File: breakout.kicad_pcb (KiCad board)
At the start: 2 copper layers, 25.9 x 20.8 mm, 12 parts, among them P1 CONN_01X08, P2 CONN_01X08, U1 ESP-12E, U2 APE8865Y5-33-HF-3

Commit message: Make vias a bit prettier.
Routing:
- net GND: track 29.0 -> 25.1 mm
- net /3V3: track 39.7 -> 43.2 mm
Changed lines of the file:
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@@
-(kicad_pcb (version 4) (host pcbnew 0.201512291232+6408~40~ubuntu15.04.1-stable)
+(kicad_pcb (version 4) (host pcbnew 4.0.1-3.201512221402+6198~38~ubuntu15.04.1-stable)
   (general
     (links 33)
     (no_connects 0)
-    (area 121.891667 43.899799 154.968334 74.325)
+    (area 125.400999 51.486999 151.459001 72.465001)
     (thickness 1.6)
     (drawings 31)
-    (tracks 144)
+    (tracks 148)
     (zones 0)
     (modules 12)
@@
     (fp_line (start -1.55 0) (end -1.55 1.55) (layer B.SilkS) (width 0.15))
     (fp_line (start -1.55 1.55) (end 1.55 1.55) (layer B.SilkS) (width 0.15))
-    (pad 1 thru_hole rect (at 0 0 180) (size 2.032 1.7272) (drill 1.016) (layers *.Cu *.Mask B.SilkS)
+    (pad 1 thru_hole oval (at 0 0 180) (size 2.032 1.7272) (drill 1.016) (layers *.Cu *.Mask B.SilkS)
       (net 1 "Net-(P1-Pad1)"))
     (pad 2 thru_hole oval (at 0 -2.54 180) (size 2.032 1.7272) (drill 1.016) (layers *.Cu *.Mask B.SilkS)
@@
   (segment (start 127.13 71.25) (end 127 71.12) (width 0.5) (layer F.Cu) (net 15) (status 30))
   (segment (start 137.01 71.12) (end 137.33 70.8) (width 0.5) (layer B.Cu) (net 15) (status 30))
-  (segment (start 146.456 66.576) (end 141.576 66.576) (width 0.5) (layer F.Cu) (net 16))
-  (segment (start 141.576 66.576) (end 141.25 66.25) (width 0.5) (layer F.Cu) (net 16))
-  (via (at 141.25 66.25) (size 1.2) (drill 0.75) (layers F.Cu B.Cu) (net 16))
-  (segment (start 146.12 71.12) (end 141.25 66.25) (width 0.5) (layer B.Cu) (net 16))
-  (segment (start 141.25 66.25) (end 140.9 65.9) (width 0.5) (layer B.Cu) (net 16))
+  (segment (start 144.741474 68.44) (end 145.590002 68.44) (width 0.5) (layer B.Cu) (net 16))
+  (segment (start 144.69 68.44) (end 144.741474 68.44) (width 0.5) (layer B.Cu) (net 16))
+  (segment (start 146.456 66.576) (end 146.456 67.626) (width 0.5) (layer F.Cu) (net 16))
+  (segment (start 148.270002 71.12) (end 146.190001 69.039999) (width 0.5) (layer B.Cu) (net 16))
+  (segment (start 141 64.75) (end 144.69 68.44) (width 0.5) (layer B.Cu) (net 16))
+  (segment (start 145.642 68.44) (end 145.590002 68.44) (width 0.5) (layer F.Cu) (net 16))
+  (segment (start 149.86 71.12) (end 148.270002 71.12) (width 0.5) (layer B.Cu) (net 16))
+  (segment (start 146.456 67.626) (end 145.642 68.44) (width 0.5) (layer F.Cu) (net 16))
+  (segment (start 140.9 64.75) (end 141 64.75) (width 0.5) (layer B.Cu) (net 16))
+  (segment (start 146.190001 69.039999) (end 145.590002 68.44) (width 0.5) (layer B.Cu) (net 16))
+  (via (at 145.590002 68.44) (size 1.2) (drill 0.75) (layers F.Cu B.Cu) (net 16))
   (segment (start 137.33 69.85) (end 136.614998 69.85) (width 0.5) (layer B.Cu) (net 16))
   (segment (start 136.614998 69.85) (end 135.87 69.105002) (width 0.5) (layer B.Cu) (net 16))
   (segment (start 135.87 69.105002) (end 135.87 65.895) (width 0.5) (layer B.Cu) (net 16))
   (segment (start 135.87 65.895) (end 135.87 64.77) (width 0.5) (layer B.Cu) (net 16))
-  (segment (start 149.86 71.12) (end 146.12 71.12) (width 0.5) (layer B.Cu) (net 16))
-  (segment (start 140.9 65.9) (end 140.9 64.75) (width 0.5) (layer B.Cu) (net 16))
   (segment (start 140.9 64.75) (end 135.89 64.75) (width 0.5) (layer B.Cu) (net 16) (status 30))
   (segment (start 135.89 64.75) (end 135.87 64.77) (width 0.5) (layer B.Cu) (net 16) (status 30))
-  (segment (start 149.86 71.12) (end 149.7076 71.12) (width 0.5) (layer B.Cu) (net 16) (status 30))
   (segment (start 140.97 64.77) (end 140.87 64.77) (width 0.5) (layer B.Cu) (net 16) (status 30))
-  (segment (start 132.5 66.5) (end 132.5 65.64) (width 0.5) (layer B.Cu) (net 17))
-  (segment (start 132.5 65.64) (end 133.37 64.77) (width 0.5) (layer B.Cu) (net 17))
-  (segment (start 130.456 66.576) (end 132.424 66.576) (width 0.5) (layer F.Cu) (net 17))
-  (segment (start 132.424 66.576) (end 132.5 66.5) (width 0.5) (layer F.Cu) (net 17))
-  (via (at 132.5 66.5) (size 1.2) (drill 0.75) (layers F.Cu B.Cu) (net 17))
+  (segment (start 131.67 67.93) (end 131.67 66.47) (width 0.5) (layer B.Cu) (net 17))
+  (segment (start 131.67 66.47) (end 133.37 64.77) (width 0.5) (layer B.Cu) (net 17))
+  (segment (start 131.69 70.29) (end 131.69 67.95) (width 0.5) (layer F.Cu) (net 17))
+  (segment (start 131.69 67.95) (end 131.67 67.93) (width 0.5) (layer F.Cu) (net 17))
+  (via (at 131.67 67.93) (size 1.2) (drill 0.75) (layers F.Cu B.Cu) (net 17))
+  (segment (start 132.65 71.25) (end 131.69 70.29) (width 0.5) (layer F.Cu) (net 17))
   (segment (start 133.2405 64.8995) (end 133.37 64.77) (width 0.5) (layer B.Cu) (net 17))
   (via (at 134.75 71.25) (size 1.2) (drill 0.75) (layers F.Cu B.Cu) (net 17))

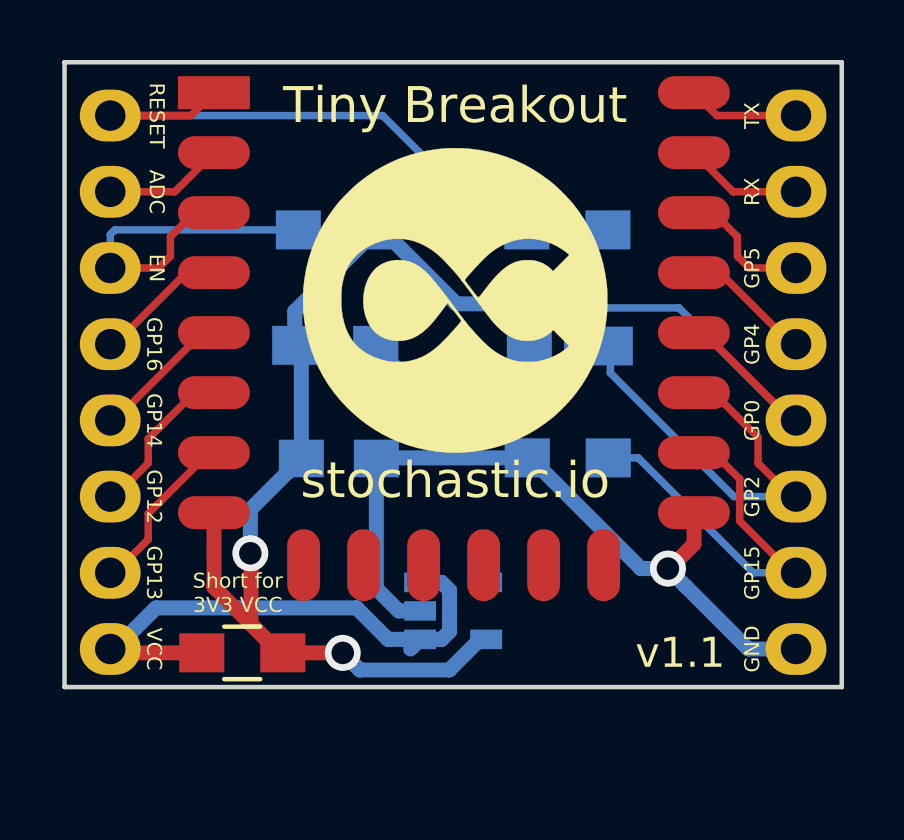
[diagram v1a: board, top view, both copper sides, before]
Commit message: Delete rogue tracks.
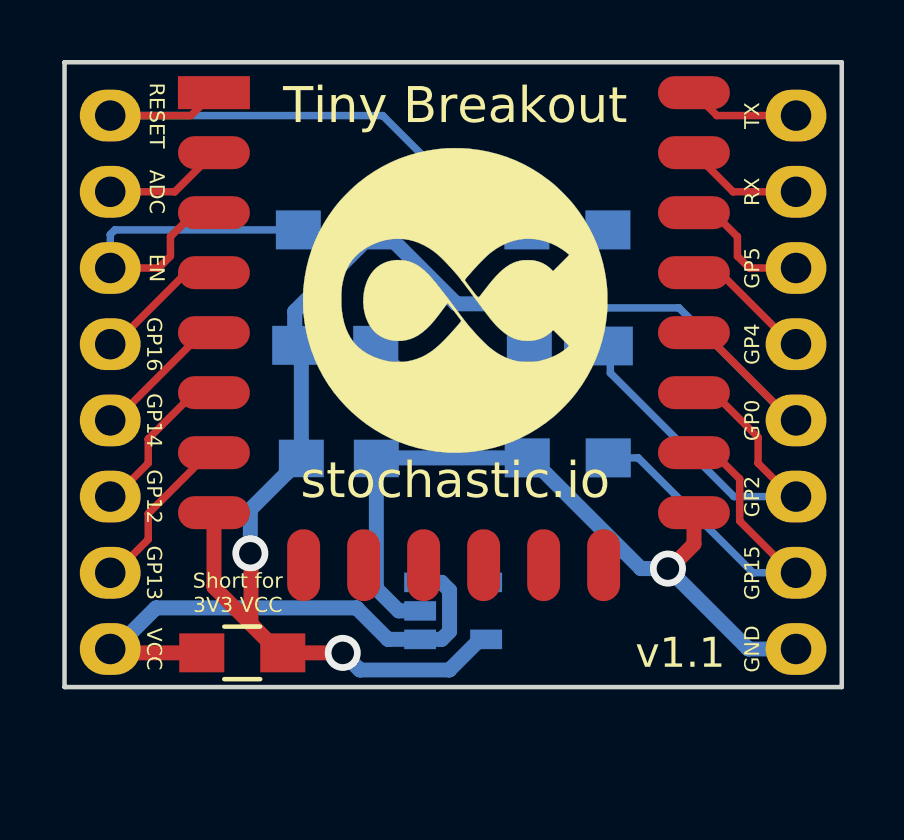
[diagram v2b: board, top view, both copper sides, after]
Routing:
- net Net-(P2-Pad5): track 24.9 -> 24.2 mm
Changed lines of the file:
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@@
     (links 33)
     (no_connects 0)
-    (area 125.400999 51.486999 151.459001 72.465001)
+    (area 121.891667 43.899799 154.968334 74.325)
     (thickness 1.6)
     (drawings 31)
-    (tracks 148)
+    (tracks 143)
     (zones 0)
     (modules 12)
@@
     (visible_elements FFFFFF7F)
     (pcbplotparams
-      (layerselection 0x010f0_ffffffff)
+      (layerselection 0x010f0_80000001)
       (usegerberextensions true)
       (excludeedgelayer true)
@@
       (drillshape 0)
       (scaleselection 1)
-      (outputdirectory ../../gerbs/))
+      (outputdirectory /home/stavros/Desktop/gerbs/))
   )
   (net 0 "")
@@
   (segment (start 147.3236 58.576) (end 146.456 58.576) (width 0.25) (layer F.Cu) (net 11) (status 30))
   (segment (start 142.954998 59.75) (end 145.9576 59.75) (width 0.25) (layer B.Cu) (net 12))
-  (segment (start 145.9576 59.75) (end 149.7076 63.5) (width 0.25) (layer B.Cu) (net 12))
-  (segment (start 149.7076 63.5) (end 149.86 63.5) (width 0.25) (layer B.Cu) (net 12))
+  (segment (start 145.9576 59.75) (end 149.7076 63.5) (width 0.25) (layer B.Cu) (net 12) (status 20))
+  (segment (start 149.7076 63.5) (end 149.86 63.5) (width 0.25) (layer B.Cu) (net 12) (status 30))
   (segment (start 142.25 62.275) (end 142.25 60.454998) (width 0.25) (layer B.Cu) (net 12))
   (segment (start 142.25 60.454998) (end 142.954998 59.75) (width 0.25) (layer B.Cu) (net 12))
-  (segment (start 135.85 61) (end 135.95 61) (width 0.25) (layer B.Cu) (net 12))
-  (segment (start 135.95 61) (end 137.95 63) (width 0.25) (layer B.Cu) (net 12))
+  (segment (start 135.85 61) (end 135.95 61) (width 0.25) (layer B.Cu) (net 12) (status 30))
+  (segment (start 135.95 61) (end 137.95 63) (width 0.25) (layer B.Cu) (net 12) (status 10))
   (segment (start 137.95 63) (end 141.525 63) (width 0.25) (layer B.Cu) (net 12))
   (segment (start 141.525 63) (end 142.25 62.275) (width 0.25) (layer B.Cu) (net 12))
-  (segment (start 135.85 61.62001) (end 135.85 61) (width 0.25) (layer B.Cu) (net 12) (status 30))
   (segment (start 146.332 60.452) (end 146.456 60.576) (width 0.25) (layer F.Cu) (net 12) (status 30))
   (segment (start 145.806 60.576) (end 146.456 60.576) (width 0.25) (layer F.Cu) (net 12) (status 30))
@@
   (segment (start 147.98101 66.85341) (end 149.7076 68.58) (width 0.25) (layer F.Cu) (net 14) (status 20))
   (segment (start 149.7076 68.58) (end 149.86 68.58) (width 0.25) (layer F.Cu) (net 14) (status 30))
-  (segment (start 137.33 70.8) (end 136.260038 70.8) (width 0.5) (layer B.Cu) (net 15))
-  (segment (start 127.1524 71.12) (end 127 71.12) (width 0.5) (layer B.Cu) (net 15))
+  (segment (start 137.33 70.8) (end 136.260038 70.8) (width 0.5) (layer B.Cu) (net 15) (status 10))
+  (segment (start 127.1524 71.12) (end 127 71.12) (width 0.5) (layer B.Cu) (net 15) (status 30))
   (segment (start 136.260038 70.8) (end 135.210038 69.75) (width 0.5) (layer B.Cu) (net 15))
-  (segment (start 128.5224 69.75) (end 127.1524 71.12) (width 0.5) (layer B.Cu) (net 15))
+  (segment (start 128.5224 69.75) (end 127.1524 71.12) (width 0.5) (layer B.Cu) (net 15) (status 20))
   (segment (start 135.210038 69.75) (end 128.5224 69.75) (width 0.5) (layer B.Cu) (net 15))
-  (segment (start 137.33 68.9) (end 138.045002 68.9) (width 0.5) (layer B.Cu) (net 15))
+  (segment (start 137.33 68.9) (end 138.045002 68.9) (width 0.5) (layer B.Cu) (net 15) (status 10))
   (segment (start 138.045002 68.9) (end 138.310001 69.164999) (width 0.5) (layer B.Cu) (net 15))
   (segment (start 138.310001 69.164999) (end 138.310001 70.535001) (width 0.5) (layer B.Cu) (net 15))
   (segment (start 138.310001 70.535001) (end 138.045002 70.8) (width 0.5) (layer B.Cu) (net 15))
-  (segment (start 138.045002 70.8) (end 137.33 70.8) (width 0.5) (layer B.Cu) (net 15))
+  (segment (start 138.045002 70.8) (end 137.33 70.8) (width 0.5) (layer B.Cu) (net 15) (status 20))
   (segment (start 130.05 71.25) (end 127.13 71.25) (width 0.5) (layer F.Cu) (net 15) (status 30))
   (segment (start 127.13 71.25) (end 127 71.12) (width 0.5) (layer F.Cu) (net 15) (status 30))
-  (segment (start 137.01 71.12) (end 137.33 70.8) (width 0.5) (layer B.Cu) (net 15) (status 30))
-  (segment (start 144.741474 68.44) (end 145.590002 68.44) (width 0.5) (layer B.Cu) (net 16))
-  (segment (start 144.69 68.44) (end 144.741474 68.44) (width 0.5) (layer B.Cu) (net 16))
-  (segment (start 146.456 66.576) (end 146.456 67.626) (width 0.5) (layer F.Cu) (net 16))
-  (segment (start 148.270002 71.12) (end 146.190001 69.039999) (width 0.5) (layer B.Cu) (net 16))
-  (segment (start 141 64.75) (end 144.69 68.44) (width 0.5) (layer B.Cu) (net 16))
+  (segment (start 144.69 68.44) (end 145.590002 68.44) (width 0.5) (layer B.Cu) (net 16))
+  (segment (start 146.456 66.576) (end 146.456 67.626) (width 0.5) (layer F.Cu) (net 16) (status 10))
+  (segment (start 148.270002 71.12) (end 145.590002 68.44) (width 0.5) (layer B.Cu) (net 16))
+  (segment (start 141 64.75) (end 144.69 68.44) (width 0.5) (layer B.Cu) (net 16) (status 10))
   (segment (start 145.642 68.44) (end 145.590002 68.44) (width 0.5) (layer F.Cu) (net 16))
-  (segment (start 149.86 71.12) (end 148.270002 71.12) (width 0.5) (layer B.Cu) (net 16))
+  (segment (start 149.86 71.12) (end 148.270002 71.12) (width 0.5) (layer B.Cu) (net 16) (status 10))
   (segment (start 146.456 67.626) (end 145.642 68.44) (width 0.5) (layer F.Cu) (net 16))
-  (segment (start 140.9 64.75) (end 141 64.75) (width 0.5) (layer B.Cu) (net 16))
-  (segment (start 146.190001 69.039999) (end 145.590002 68.44) (width 0.5) (layer B.Cu) (net 16))
+  (segment (start 140.9 64.75) (end 141 64.75) (width 0.5) (layer B.Cu) (net 16) (status 30))
   (via (at 145.590002 68.44) (size 1.2) (drill 0.75) (layers F.Cu B.Cu) (net 16))
-  (segment (start 137.33 69.85) (end 136.614998 69.85) (width 0.5) (layer B.Cu) (net 16))
+  (segment (start 137.33 69.85) (end 136.614998 69.85) (width 0.5) (layer B.Cu) (net 16) (status 10))
   (segment (start 136.614998 69.85) (end 135.87 69.105002) (width 0.5) (layer B.Cu) (net 16))
-  (segment (start 135.87 69.105002) (end 135.87 65.895) (width 0.5) (layer B.Cu) (net 16))
-  (segment (start 135.87 65.895) (end 135.87 64.77) (width 0.5) (layer B.Cu) (net 16))
+  (segment (start 135.87 69.105002) (end 135.87 64.77) (width 0.5) (layer B.Cu) (net 16) (status 20))
   (segment (start 140.9 64.75) (end 135.89 64.75) (width 0.5) (layer B.Cu) (net 16) (status 30))
   (segment (start 135.89 64.75) (end 135.87 64.77) (width 0.5) (layer B.Cu) (net 16) (status 30))
   (segment (start 140.97 64.77) (end 140.87 64.77) (width 0.5) (layer B.Cu) (net 16) (status 30))
   (segment (start 131.67 67.93) (end 131.67 66.47) (width 0.5) (layer B.Cu) (net 17))
-  (segment (start 131.67 66.47) (end 133.37 64.77) (width 0.5) (layer B.Cu) (net 17))
+  (segment (start 131.67 66.47) (end 133.37 64.77) (width 0.5) (layer B.Cu) (net 17) (status 20))
   (segment (start 131.69 70.29) (end 131.69 67.95) (width 0.5) (layer F.Cu) (net 17))
   (segment (start 131.69 67.95) (end 131.67 67.93) (width 0.5) (layer F.Cu) (net 17))
   (via (at 131.67 67.93) (size 1.2) (drill 0.75) (layers F.Cu B.Cu) (net 17))
-  (segment (start 132.65 71.25) (end 131.69 70.29) (width 0.5) (layer F.Cu) (net 17))
-  (segment (start 133.2405 64.8995) (end 133.37 64.77) (width 0.5) (layer B.Cu) (net 17))
+  (segment (start 132.65 71.25) (end 131.69 70.29) (width 0.5) (layer F.Cu) (net 17) (status 10))
+  (segment (start 133.2405 64.8995) (end 133.37 64.77) (width 0.5) (layer B.Cu) (net 17) (status 30))
   (via (at 134.75 71.25) (size 1.2) (drill 0.75) (layers F.Cu B.Cu) (net 17))
-  (segment (start 132.75 71.25) (end 134.75 71.25) (width 0.5) (layer F.Cu) (net 17))
-  (segment (start 139.53 70.8) (end 139.325 70.8) (width 0.5) (layer B.Cu) (net 17))
+  (segment (start 132.75 71.25) (end 134.75 71.25) (width 0.5) (layer F.Cu) (net 17) (status 10))
+  (segment (start 139.53 70.8) (end 139.325 70.8) (width 0.5) (layer B.Cu) (net 17) (status 30))
   (segment (start 138.304992 71.820008) (end 135.320008 71.820008) (width 0.5) (layer B.Cu) (net 17))
-  (segment (start 139.325 70.8) (end 138.304992 71.820008) (width 0.5) (layer B.Cu) (net 17))
+  (segment (start 139.325 70.8) (end 138.304992 71.820008) (width 0.5) (layer B.Cu) (net 17) (status 10))
   (segment (start 135.320008 71.820008) (end 134.75 71.25) (width 0.5) (layer B.Cu) (net 17))
   (segment (start 141.025999 59.614001) (end 140.5 59.614001) (width 0.5) (layer B.Cu) (net 17))

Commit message: Make it more Web 2.0.
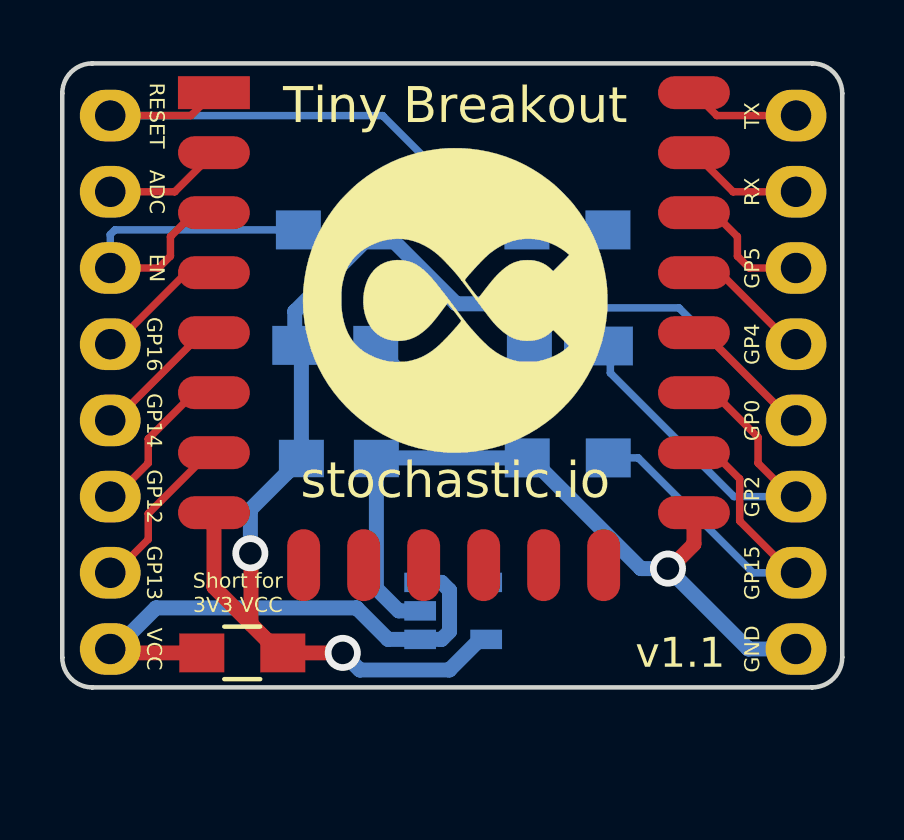
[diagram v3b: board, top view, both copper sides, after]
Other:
- board size 25.9 x 20.8 mm -> 26 x 20.8 mm
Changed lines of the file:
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@@
     (area 121.891667 43.899799 154.968334 74.325)
     (thickness 1.6)
-    (drawings 31)
+    (drawings 35)
     (tracks 143)
     (zones 0)
@@
     )
   )
+  (gr_arc (start 126.4 71.4) (end 126.4 72.4) (angle 90) (layer Edge.Cuts) (width 0.15))
+  (gr_arc (start 150.4 71.4) (end 151.4 71.4) (angle 90) (layer Edge.Cuts) (width 0.15))
+  (gr_arc (start 150.4 52.6) (end 150.4 51.6) (angle 90) (layer Edge.Cuts) (width 0.15))
+  (gr_arc (start 126.4 52.6) (end 125.4 52.6) (angle 90) (layer Edge.Cuts) (width 0.15))
   (gr_text R6 (at 134.5 59.25) (layer B.SilkS)
     (effects (font (size 1 1) (thickness 0.25)) (justify mirror))
@@
     (effects (font (size 1 1) (thickness 0.25)) (justify mirror))
   )
-  (gr_line (start 125.476 72.39) (end 125.476 51.562) (layer Edge.Cuts) (width 0.15))
-  (gr_line (start 151.384 72.39) (end 125.476 72.39) (layer Edge.Cuts) (width 0.15))
-  (gr_line (start 151.384 51.562) (end 151.384 72.39) (layer Edge.Cuts) (width 0.15))
-  (gr_line (start 125.476 51.562) (end 151.384 51.562) (layer Edge.Cuts) (width 0.15))
+  (gr_line (start 125.4 71.4) (end 125.4 52.6) (layer Edge.Cuts) (width 0.15))
+  (gr_line (start 150.4 72.4) (end 126.4 72.4) (layer Edge.Cuts) (width 0.15))
+  (gr_line (start 151.4 52.6) (end 151.4 71.4) (layer Edge.Cuts) (width 0.15))
+  (gr_line (start 126.4 51.6) (end 150.4 51.6) (layer Edge.Cuts) (width 0.15))
   (segment (start 140.89 57.15) (end 139.89 57.15) (width 0.25) (layer B.Cu) (net 1) (status 10))
   (segment (start 139.89 57.15) (end 136.08 53.34) (width 0.25) (layer B.Cu) (net 1))

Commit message: Add pin.
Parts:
- removed R5: 0Ω, Resistors_SMD:R_0805_HandSoldering
- P1, P2: value CONN_01X08 -> CONN_01X09; footprint Pin_Headers:Pin_Header_Straight_1x08 -> Pin_Headers:Pin_Header_Straight_1x09
- moved U1 0.41 mm to (130.1, 52.6)
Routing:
- net /3V3: track 43.2 -> 50.6 mm
- net +12V: track 18.0 -> 15.1 mm
- net GND: track 25.1 -> 27.6 mm
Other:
- board size 26 x 20.8 mm -> 26 x 23.8 mm
- board text added: "3.3V"
- board text added: "v1.2"
- board text removed: "Short for 3V3 VCC"
- board text removed: "v1.1"

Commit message: Rewire everything.
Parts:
- moved R6 8.68 mm to (142.3, 57.2)
- moved R2 7.80 mm to (134.4, 57.1)
- moved U1 4.24 mm to (130.4, 56.8)
- moved R1 3.81 mm to (134.4, 61.0)
- moved C1 0.20 mm to (134.4, 64.8)
- turned U2 to 180 degrees
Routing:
- net /3V3: track 50.6 -> 34.2 mm, vias 2 -> 1
- net Net-(P2-Pad5): track 24.2 -> 13.9 mm
- net Net-(P1-Pad1): track 19.3 -> 13.1 mm
- net GND: track 27.6 -> 31.9 mm
- net Net-(P2-Pad7): track 15.6 -> 11.4 mm
- net +12V: track 15.1 -> 17.5 mm
- net Net-(P1-Pad3): track 14.0 -> 11.6 mm
- net Net-(P2-Pad6): track 14.8 -> 12.6 mm
- net Net-(P1-Pad7): track 5.62 -> 3.49 mm
- net Net-(P2-Pad1): track 3.72 -> 5.63 mm
- net Net-(P1-Pad6): track 5.37 -> 3.71 mm
- net Net-(P1-Pad5): track 4.67 -> 3.94 mm
- net Net-(P2-Pad2): track 3.94 -> 4.67 mm
- net Net-(P1-Pad2): track 4.00 -> 4.61 mm
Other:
- board text added: "<16V"
- board text added: "stavros.io"
- board text removed: "VCC"
- board text removed: "stochastic.io"
